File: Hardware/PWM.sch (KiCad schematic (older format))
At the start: 7 parts, among them P1 PWM, U1 NLAS4599

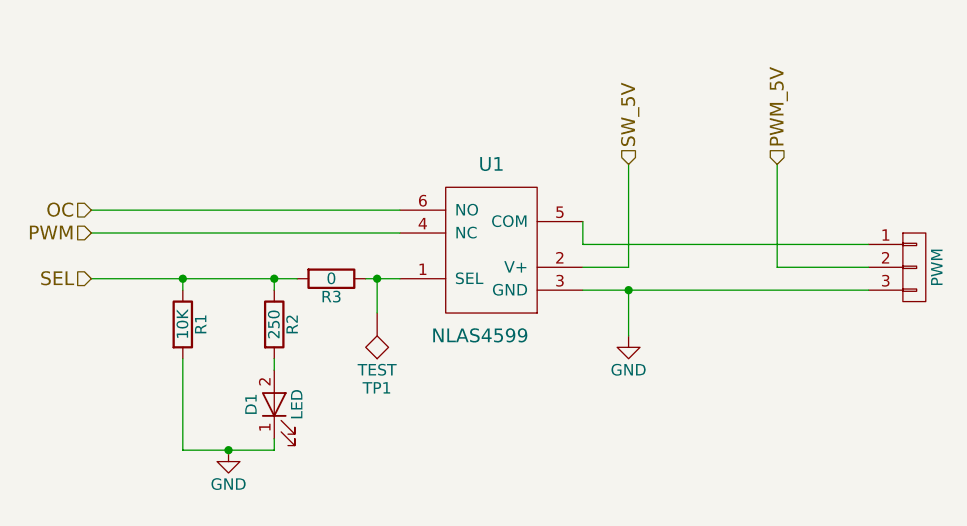
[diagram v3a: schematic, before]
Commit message: Added F0 chip
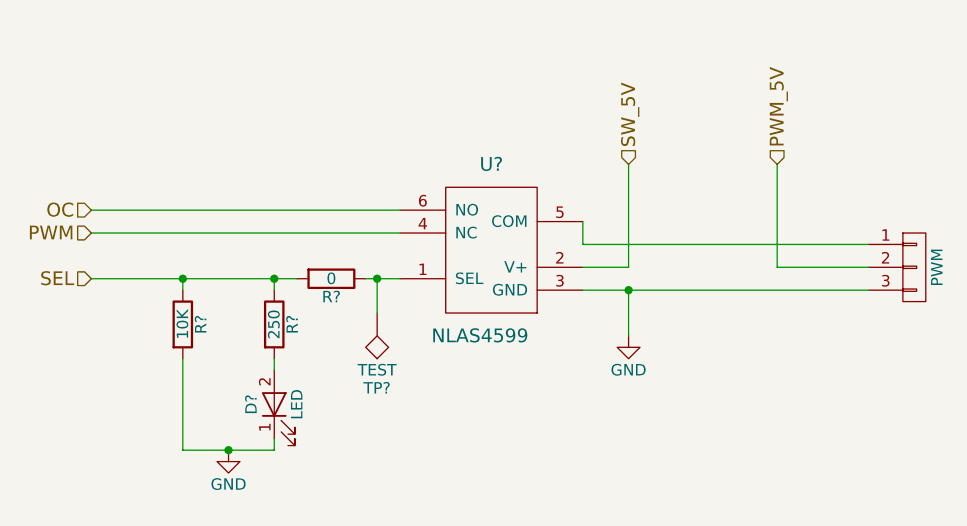
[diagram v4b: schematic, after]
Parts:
- renumbered D1 to D?, P1 to P?, R2 to R?, R34 to R?, R36 to R?, TP12 to TP?, U1 to U?
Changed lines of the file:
@@
 $Descr A4 11693 8268
 encoding utf-8
-Sheet 3 17
+Sheet 8 18
 Title "PWM Switching Circuit"
 Date "2017-05-13"
@@
 U 1 1 5917D576
 P 6350 2400
-AR Path="/5917CEAC/5917D576" Ref="P?"  Part="1"
-AR Path="/5917EAD8/5917D576" Ref="P?"  Part="1"
-AR Path="/5917F7DD/5917D576" Ref="P?"  Part="1"
-AR Path="/591836F4/5917D576" Ref="P?"  Part="1"
-AR Path="/5919E173/5917D576" Ref="P?"  Part="1"
-AR Path="/591E6415/591EA448/5917D576" Ref="P1"  Part="1"
-AR Path="/591E6415/591EA45A/5917D576" Ref="P2"  Part="1"
-AR Path="/591E6415/591EA50E/5917D576" Ref="P12"  Part="1"
-AR Path="/591E6415/591EA490/5917D576" Ref="P5"  Part="1"
-AR Path="/591E6415/591EA46C/5917D576" Ref="P3"  Part="1"
-AR Path="/591E6415/591EA47E/5917D576" Ref="P4"  Part="1"
-AR Path="/591E6415/591EA4A2/5917D576" Ref="P6"  Part="1"
-AR Path="/591E6415/591EA4B4/5917D576" Ref="P7"  Part="1"
-AR Path="/591E6415/591EA4C6/5917D576" Ref="P8"  Part="1"
-AR Path="/591E6415/591EA4D8/5917D576" Ref="P9"  Part="1"
-AR Path="/591E6415/591EA4EA/5917D576" Ref="P10"  Part="1"
-AR Path="/591E6415/591EA4FC/5917D576" Ref="P11"  Part="1"
-F 0 "P1" H 6350 2600 50  0001 C CNN
+F 0 "P?" H 6350 2600 50  0001 C CNN
 F 1 "PWM" V 6450 2400 50  0000 C CNN
 F 2 "" H 6350 2400 50  0000 C CNN
@@
 $EndComp
 $Comp
-L NLAS4599 U1
+L NLAS4599 U?
 U 1 1 5917D57C
 P 4500 2600
-AR Path="/5917CEAC/5917D57C" Ref="U1"  Part="1"
-AR Path="/5917EAD8/5917D57C" Ref="U1"  Part="1"
-AR Path="/5917F7DD/5917D57C" Ref="U1"  Part="1"
-AR Path="/591836F4/5917D57C" Ref="U1"  Part="1"
-AR Path="/5919E173/5917D57C" Ref="U1"  Part="1"
-AR Path="/591E6415/591EA448/5917D57C" Ref="U?"  Part="1"
-AR Path="/591E6415/591EA45A/5917D57C" Ref="U1"  Part="1"
-AR Path="/591E6415/591EA50E/5917D57C" Ref="U1"  Part="1"
-AR Path="/591E6415/591EA490/5917D57C" Ref="U1"  Part="1"
-AR Path="/591E6415/591EA46C/5917D57C" Ref="U1"  Part="1"
-AR Path="/591E6415/591EA47E/5917D57C" Ref="U1"  Part="1"
-AR Path="/591E6415/591EA4A2/5917D57C" Ref="U1"  Part="1"
-AR Path="/591E6415/591EA4B4/5917D57C" Ref="U1"  Part="1"
-AR Path="/591E6415/591EA4C6/5917D57C" Ref="U1"  Part="1"
-AR Path="/591E6415/591EA4D8/5917D57C" Ref="U1"  Part="1"
-AR Path="/591E6415/591EA4EA/5917D57C" Ref="U1"  Part="1"
-AR Path="/591E6415/591EA4FC/5917D57C" Ref="U1"  Part="1"
 F 0 "U?" H 4500 3250 60  0000 C CNN
 F 1 "NLAS4599" H 4550 2500 60  0000 C CNN
@@
 U 1 1 5917D836
 P 5100 2700
-AR Path="/5917CEAC/5917D836" Ref="#PWR?"  Part="1"
-AR Path="/5917EAD8/5917D836" Ref="#PWR?"  Part="1"
-AR Path="/5917F7DD/5917D836" Ref="#PWR?"  Part="1"
-AR Path="/591836F4/5917D836" Ref="#PWR?"  Part="1"
-AR Path="/5919E173/5917D836" Ref="#PWR?"  Part="1"
-AR Path="/591E6415/591EA448/5917D836" Ref="#PWR2"  Part="1"
-AR Path="/591E6415/591EA45A/5917D836" Ref="#PWR4"  Part="1"
-AR Path="/591E6415/591EA50E/5917D836" Ref="#PWR24"  Part="1"
-AR Path="/591E6415/591EA490/5917D836" Ref="#PWR10"  Part="1"
-AR Path="/591E6415/591EA46C/5917D836" Ref="#PWR6"  Part="1"
-AR Path="/591E6415/591EA47E/5917D836" Ref="#PWR8"  Part="1"
-AR Path="/591E6415/591EA4A2/5917D836" Ref="#PWR12"  Part="1"
-AR Path="/591E6415/591EA4B4/5917D836" Ref="#PWR14"  Part="1"
-AR Path="/591E6415/591EA4C6/5917D836" Ref="#PWR16"  Part="1"
-AR Path="/591E6415/591EA4D8/5917D836" Ref="#PWR18"  Part="1"
-AR Path="/591E6415/591EA4EA/5917D836" Ref="#PWR20"  Part="1"
-AR Path="/591E6415/591EA4FC/5917D836" Ref="#PWR22"  Part="1"
-F 0 "#PWR2" H 5100 2450 50  0001 C CNN
+F 0 "#PWR?" H 5100 2450 50  0001 C CNN
 F 1 "GND" H 5100 2550 50  0000 C CNN
 F 2 "" H 5100 2700 50  0000 C CNN
@@
 	4900 2300 6150 2300
 $Comp
-L LED D1
+L LED D?
 U 1 1 591EF19A
 P 3550 3000
-AR Path="/591E6415/591EA448/591EF19A" Ref="D1"  Part="1"
-AR Path="/591E6415/591EA50E/591EF19A" Ref="D12"  Part="1"
-AR Path="/591E6415/591EA490/591EF19A" Ref="D5"  Part="1"
-AR Path="/591E6415/591EA45A/591EF19A" Ref="D2"  Part="1"
-AR Path="/591E6415/591EA46C/591EF19A" Ref="D3"  Part="1"
-AR Path="/591E6415/591EA47E/591EF19A" Ref="D4"  Part="1"
-AR Path="/591E6415/591EA4A2/591EF19A" Ref="D6"  Part="1"
-AR Path="/591E6415/591EA4B4/591EF19A" Ref="D7"  Part="1"
-AR Path="/591E6415/591EA4C6/591EF19A" Ref="D8"  Part="1"
-AR Path="/591E6415/591EA4D8/591EF19A" Ref="D9"  Part="1"
-AR Path="/591E6415/591EA4EA/591EF19A" Ref="D10"  Part="1"
-AR Path="/591E6415/591EA4FC/591EF19A" Ref="D11"  Part="1"
-F 0 "D1" H 3550 3100 50  0000 C CNN
+F 0 "D?" H 3550 3100 50  0000 C CNN
 F 1 "LED" H 3550 2900 50  0000 C CNN
 F 2 "" H 3550 3000 50  0000 C CNN
@@
 $EndComp
 $Comp
-L R R2
+L R R?
 U 1 1 591EF2D3
 P 3550 2650
-AR Path="/591E6415/591EA448/591EF2D3" Ref="R2"  Part="1"
-AR Path="/591E6415/591EA50E/591EF2D3" Ref="R35"  Part="1"
-AR Path="/591E6415/591EA490/591EF2D3" Ref="R14"  Part="1"
-AR Path="/591E6415/591EA45A/591EF2D3" Ref="R5"  Part="1"
-AR Path="/591E6415/591EA46C/591EF2D3" Ref="R8"  Part="1"
-AR Path="/591E6415/591EA47E/591EF2D3" Ref="R11"  Part="1"
-AR Path="/591E6415/591EA4A2/591EF2D3" Ref="R17"  Part="1"
-AR Path="/591E6415/591EA4B4/591EF2D3" Ref="R20"  Part="1"
-AR Path="/591E6415/591EA4C6/591EF2D3" Ref="R23"  Part="1"
-AR Path="/591E6415/591EA4D8/591EF2D3" Ref="R26"  Part="1"
-AR Path="/591E6415/591EA4EA/591EF2D3" Ref="R29"  Part="1"
-AR Path="/591E6415/591EA4FC/591EF2D3" Ref="R32"  Part="1"
-F 0 "R2" V 3630 2650 50  0000 C CNN
+F 0 "R?" V 3630 2650 50  0000 C CNN
 F 1 "250" V 3550 2650 50  0000 C CNN
 F 2 "" V 3480 2650 50  0000 C CNN
@@
 Connection ~ 3550 2450
 $Comp
-L GND #PWR1
+L GND #PWR?
 U 1 1 591EF3D9
 P 3350 3200
-AR Path="/591E6415/591EA448/591EF3D9" Ref="#PWR1"  Part="1"
-AR Path="/591E6415/591EA50E/591EF3D9" Ref="#PWR23"  Part="1"
-AR Path="/591E6415/591EA490/591EF3D9" Ref="#PWR9"  Part="1"
-AR Path="/591E6415/591EA45A/591EF3D9" Ref="#PWR3"  Part="1"
-AR Path="/591E6415/591EA46C/591EF3D9" Ref="#PWR5"  Part="1"
-AR Path="/591E6415/591EA47E/591EF3D9" Ref="#PWR7"  Part="1"
-AR Path="/591E6415/591EA4A2/591EF3D9" Ref="#PWR11"  Part="1"
-AR Path="/591E6415/591EA4B4/591EF3D9" Ref="#PWR13"  Part="1"
-AR Path="/591E6415/591EA4C6/591EF3D9" Ref="#PWR15"  Part="1"
-AR Path="/591E6415/591EA4D8/591EF3D9" Ref="#PWR17"  Part="1"
-AR Path="/591E6415/591EA4EA/591EF3D9" Ref="#PWR19"  Part="1"
-AR Path="/591E6415/591EA4FC/591EF3D9" Ref="#PWR21"  Part="1"
-F 0 "#PWR1" H 3350 2950 50  0001 C CNN
+F 0 "#PWR?" H 3350 2950 50  0001 C CNN
 F 1 "GND" H 3350 3050 50  0000 C CNN
 F 2 "" H 3350 3200 50  0000 C CNN
@@
 	3550 3200 3550 3150
 $Comp
-L R R34
+L R R?
 U 1 1 591F0A89
 P 3150 2650
-AR Path="/591E6415/591EA50E/591F0A89" Ref="R34"  Part="1"
-AR Path="/591E6415/591EA448/591F0A89" Ref="R1"  Part="1"
-AR Path="/591E6415/591EA45A/591F0A89" Ref="R4"  Part="1"
-AR Path="/591E6415/591EA46C/591F0A89" Ref="R7"  Part="1"
-AR Path="/591E6415/591EA47E/591F0A89" Ref="R10"  Part="1"
-AR Path="/591E6415/591EA490/591F0A89" Ref="R13"  Part="1"
-AR Path="/591E6415/591EA4A2/591F0A89" Ref="R16"  Part="1"
-AR Path="/591E6415/591EA4B4/591F0A89" Ref="R19"  Part="1"
-AR Path="/591E6415/591EA4C6/591F0A89" Ref="R22"  Part="1"
-AR Path="/591E6415/591EA4D8/591F0A89" Ref="R25"  Part="1"
-AR Path="/591E6415/591EA4EA/591F0A89" Ref="R28"  Part="1"
-AR Path="/591E6415/591EA4FC/591F0A89" Ref="R31"  Part="1"
-F 0 "R1" V 3230 2650 50  0000 C CNN
+F 0 "R?" V 3230 2650 50  0000 C CNN
 F 1 "10K" V 3150 2650 50  0000 C CNN
 F 2 "" V 3080 2650 50  0000 C CNN
@@
 Connection ~ 3150 2450
 $Comp
-L R R36
+L R R?
 U 1 1 591F0BAE
 P 3800 2450
-AR Path="/591E6415/591EA50E/591F0BAE" Ref="R36"  Part="1"
-AR Path="/591E6415/591EA448/591F0BAE" Ref="R3"  Part="1"
-AR Path="/591E6415/591EA45A/591F0BAE" Ref="R6"  Part="1"
-AR Path="/591E6415/591EA46C/591F0BAE" Ref="R9"  Part="1"
-AR Path="/591E6415/591EA47E/591F0BAE" Ref="R12"  Part="1"
-AR Path="/591E6415/591EA490/591F0BAE" Ref="R15"  Part="1"
-AR Path="/591E6415/591EA4A2/591F0BAE" Ref="R18"  Part="1"
-AR Path="/591E6415/591EA4B4/591F0BAE" Ref="R21"  Part="1"
-AR Path="/591E6415/591EA4C6/591F0BAE" Ref="R24"  Part="1"
-AR Path="/591E6415/591EA4D8/591F0BAE" Ref="R27"  Part="1"
-AR Path="/591E6415/591EA4EA/591F0BAE" Ref="R30"  Part="1"
-AR Path="/591E6415/591EA4FC/591F0BAE" Ref="R33"  Part="1"
-F 0 "R3" V 3880 2450 50  0000 C CNN
+F 0 "R?" V 3880 2450 50  0000 C CNN
 F 1 "0" V 3800 2450 50  0000 C CNN
 F 2 "" V 3730 2450 50  0000 C CNN
@@
 Connection ~ 4000 2450
 $Comp
-L TEST TP12
+L TEST TP?
 U 1 1 591F0CEF
 P 4000 2600
-AR Path="/591E6415/591EA50E/591F0CEF" Ref="TP12"  Part="1"
-AR Path="/591E6415/591EA448/591F0CEF" Ref="TP1"  Part="1"
-AR Path="/591E6415/591EA45A/591F0CEF" Ref="TP2"  Part="1"
-AR Path="/591E6415/591EA46C/591F0CEF" Ref="TP3"  Part="1"
-AR Path="/591E6415/591EA47E/591F0CEF" Ref="TP4"  Part="1"
-AR Path="/591E6415/591EA490/591F0CEF" Ref="TP5"  Part="1"
-AR Path="/591E6415/591EA4A2/591F0CEF" Ref="TP6"  Part="1"
-AR Path="/591E6415/591EA4B4/591F0CEF" Ref="TP7"  Part="1"
-AR Path="/591E6415/591EA4C6/591F0CEF" Ref="TP8"  Part="1"
-AR Path="/591E6415/591EA4D8/591F0CEF" Ref="TP9"  Part="1"
-AR Path="/591E6415/591EA4EA/591F0CEF" Ref="TP10"  Part="1"
-AR Path="/591E6415/591EA4FC/591F0CEF" Ref="TP11"  Part="1"
-F 0 "TP1" H 4000 2900 50  0000 C BNN
+F 0 "TP?" H 4000 2900 50  0000 C BNN
 F 1 "TEST" H 4000 2850 50  0000 C CNN
 F 2 "" H 4000 2600 50  0000 C CNN

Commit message: Added F7 Circuitry
Added way too much for 1 commit.
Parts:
- gave numbers to parts that had none: 7
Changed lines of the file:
@@
 LIBS:contrib
 LIBS:valves
+LIBS:ZeroPilot-cache
 EELAYER 25 0
 EELAYER END
 $Descr A4 11693 8268
 encoding utf-8
-Sheet 8 18
+Sheet 6 17
 Title "PWM Switching Circuit"
 Date "2017-05-13"
@@
 $EndDescr
 $Comp
-L CONN_01X03 P?
+L CONN_01X03 P1
 U 1 1 5917D576
 P 6350 2400
-F 0 "P?" H 6350 2600 50  0001 C CNN
+AR Path="/591E6415/591EA448/5917D576" Ref="P1"  Part="1"
+AR Path="/591E6415/591EA45A/5917D576" Ref="P2"  Part="1"
+AR Path="/591E6415/591EA46C/5917D576" Ref="P3"  Part="1"
+AR Path="/591E6415/591EA47E/5917D576" Ref="P4"  Part="1"
+AR Path="/591E6415/591EA490/5917D576" Ref="P5"  Part="1"
+AR Path="/591E6415/591EA4A2/5917D576" Ref="P6"  Part="1"
+AR Path="/591E6415/591EA4B4/5917D576" Ref="P7"  Part="1"
+AR Path="/591E6415/591EA4C6/5917D576" Ref="P8"  Part="1"
+AR Path="/591E6415/591EA4D8/5917D576" Ref="P9"  Part="1"
+AR Path="/591E6415/591EA4EA/5917D576" Ref="P10"  Part="1"
+AR Path="/591E6415/591EA4FC/5917D576" Ref="P11"  Part="1"
+AR Path="/591E6415/591EA50E/5917D576" Ref="P12"  Part="1"
+F 0 "P4" H 6350 2600 50  0001 C CNN
 F 1 "PWM" V 6450 2400 50  0000 C CNN
 F 2 "" H 6350 2400 50  0000 C CNN
@@
 $EndComp
 $Comp
-L NLAS4599 U?
+L NLAS4599 U1
 U 1 1 5917D57C
 P 4500 2600
-F 0 "U?" H 4500 3250 60  0000 C CNN
+AR Path="/591E6415/591EA448/5917D57C" Ref="U1"  Part="1"
+AR Path="/591E6415/591EA45A/5917D57C" Ref="U2"  Part="1"
+AR Path="/591E6415/591EA46C/5917D57C" Ref="U3"  Part="1"
+AR Path="/591E6415/591EA47E/5917D57C" Ref="U4"  Part="1"
+AR Path="/591E6415/591EA490/5917D57C" Ref="U5"  Part="1"
+AR Path="/591E6415/591EA4A2/5917D57C" Ref="U6"  Part="1"
+AR Path="/591E6415/591EA4B4/5917D57C" Ref="U7"  Part="1"
+AR Path="/591E6415/591EA4C6/5917D57C" Ref="U8"  Part="1"
+AR Path="/591E6415/591EA4D8/5917D57C" Ref="U9"  Part="1"
+AR Path="/591E6415/591EA4EA/5917D57C" Ref="U10"  Part="1"
+AR Path="/591E6415/591EA4FC/5917D57C" Ref="U11"  Part="1"
+AR Path="/591E6415/591EA50E/5917D57C" Ref="U12"  Part="1"
+F 0 "U4" H 4500 3250 60  0000 C CNN
 F 1 "NLAS4599" H 4550 2500 60  0000 C CNN
 F 2 "" H 4300 2350 60  0001 C CNN
@@
 	4900 2500 6150 2500
 $Comp
-L GND #PWR?
+L GND #PWR01
 U 1 1 5917D836
 P 5100 2700
-F 0 "#PWR?" H 5100 2450 50  0001 C CNN
+AR Path="/591E6415/591EA448/5917D836" Ref="#PWR01"  Part="1"
+AR Path="/591E6415/591EA45A/5917D836" Ref="#PWR03"  Part="1"
+AR Path="/591E6415/591EA46C/5917D836" Ref="#PWR05"  Part="1"
+AR Path="/591E6415/591EA47E/5917D836" Ref="#PWR07"  Part="1"
+AR Path="/591E6415/591EA490/5917D836" Ref="#PWR09"  Part="1"
+AR Path="/591E6415/591EA4A2/5917D836" Ref="#PWR011"  Part="1"
+AR Path="/591E6415/591EA4B4/5917D836" Ref="#PWR013"  Part="1"
+AR Path="/591E6415/591EA4C6/5917D836" Ref="#PWR015"  Part="1"
+AR Path="/591E6415/591EA4D8/5917D836" Ref="#PWR017"  Part="1"
+AR Path="/591E6415/591EA4EA/5917D836" Ref="#PWR019"  Part="1"
+AR Path="/591E6415/591EA4FC/5917D836" Ref="#PWR021"  Part="1"
+AR Path="/591E6415/591EA50E/5917D836" Ref="#PWR023"  Part="1"
+F 0 "#PWR07" H 5100 2450 50  0001 C CNN
 F 1 "GND" H 5100 2550 50  0000 C CNN
 F 2 "" H 5100 2700 50  0000 C CNN
@@
 	5750 2400 5750 1950
 Connection ~ 5100 2500
-Wire Wire Line
-	4900 2400 5100 2400
 Wire Wire Line
 	5100 2700 5100 2500
@@
 	4900 2300 6150 2300
 $Comp
-L LED D?
+L LED D1
 U 1 1 591EF19A
 P 3550 3000
-F 0 "D?" H 3550 3100 50  0000 C CNN
+AR Path="/591E6415/591EA448/591EF19A" Ref="D1"  Part="1"
+AR Path="/591E6415/591EA45A/591EF19A" Ref="D2"  Part="1"
+AR Path="/591E6415/591EA46C/591EF19A" Ref="D3"  Part="1"
+AR Path="/591E6415/591EA47E/591EF19A" Ref="D4"  Part="1"
+AR Path="/591E6415/591EA490/591EF19A" Ref="D5"  Part="1"
+AR Path="/591E6415/591EA4A2/591EF19A" Ref="D6"  Part="1"
+AR Path="/591E6415/591EA4B4/591EF19A" Ref="D7"  Part="1"
+AR Path="/591E6415/591EA4C6/591EF19A" Ref="D8"  Part="1"
+AR Path="/591E6415/591EA4D8/591EF19A" Ref="D9"  Part="1"
+AR Path="/591E6415/591EA4EA/591EF19A" Ref="D10"  Part="1"
+AR Path="/591E6415/591EA4FC/591EF19A" Ref="D11"  Part="1"
+AR Path="/591E6415/591EA50E/591EF19A" Ref="D12"  Part="1"
+F 0 "D4" H 3550 3100 50  0000 C CNN
 F 1 "LED" H 3550 2900 50  0000 C CNN
 F 2 "" H 3550 3000 50  0000 C CNN
@@
 $EndComp
 $Comp
-L R R?
+L R R2
 U 1 1 591EF2D3
 P 3550 2650
-F 0 "R?" V 3630 2650 50  0000 C CNN
+AR Path="/591E6415/591EA448/591EF2D3" Ref="R2"  Part="1"
+AR Path="/591E6415/591EA45A/591EF2D3" Ref="R5"  Part="1"
+AR Path="/591E6415/591EA46C/591EF2D3" Ref="R8"  Part="1"
+AR Path="/591E6415/591EA47E/591EF2D3" Ref="R11"  Part="1"
+AR Path="/591E6415/591EA490/591EF2D3" Ref="R14"  Part="1"
+AR Path="/591E6415/591EA4A2/591EF2D3" Ref="R17"  Part="1"
+AR Path="/591E6415/591EA4B4/591EF2D3" Ref="R20"  Part="1"
+AR Path="/591E6415/591EA4C6/591EF2D3" Ref="R23"  Part="1"
+AR Path="/591E6415/591EA4D8/591EF2D3" Ref="R26"  Part="1"
+AR Path="/591E6415/591EA4EA/591EF2D3" Ref="R29"  Part="1"
+AR Path="/591E6415/591EA4FC/591EF2D3" Ref="R32"  Part="1"
+AR Path="/591E6415/591EA50E/591EF2D3" Ref="R35"  Part="1"
+F 0 "R11" V 3630 2650 50  0000 C CNN
 F 1 "250" V 3550 2650 50  0000 C CNN
 F 2 "" V 3480 2650 50  0000 C CNN
@@
 Connection ~ 3550 2450
 $Comp
-L GND #PWR?
+L GND #PWR02
 U 1 1 591EF3D9
-P 3350 3200
-F 0 "#PWR?" H 3350 2950 50  0001 C CNN
-F 1 "GND" H 3350 3050 50  0000 C CNN
-F 2 "" H 3350 3200 50  0000 C CNN
-F 3 "" H 3350 3200 50  0000 C CNN
-	1    3350 3200
+P 3350 3250
+AR Path="/591E6415/591EA448/591EF3D9" Ref="#PWR02"  Part="1"
+AR Path="/591E6415/591EA45A/591EF3D9" Ref="#PWR04"  Part="1"
+AR Path="/591E6415/591EA46C/591EF3D9" Ref="#PWR06"  Part="1"
+AR Path="/591E6415/591EA47E/591EF3D9" Ref="#PWR08"  Part="1"
+AR Path="/591E6415/591EA490/591EF3D9" Ref="#PWR010"  Part="1"
+AR Path="/591E6415/591EA4A2/591EF3D9" Ref="#PWR012"  Part="1"
+AR Path="/591E6415/591EA4B4/591EF3D9" Ref="#PWR014"  Part="1"
+AR Path="/591E6415/591EA4C6/591EF3D9" Ref="#PWR016"  Part="1"
+AR Path="/591E6415/591EA4D8/591EF3D9" Ref="#PWR018"  Part="1"
+AR Path="/591E6415/591EA4EA/591EF3D9" Ref="#PWR020"  Part="1"
+AR Path="/591E6415/591EA4FC/591EF3D9" Ref="#PWR022"  Part="1"
+AR Path="/591E6415/591EA50E/591EF3D9" Ref="#PWR024"  Part="1"
+F 0 "#PWR08" H 3350 3000 50  0001 C CNN
+F 1 "GND" H 3350 3100 50  0000 C CNN
+F 2 "" H 3350 3250 50  0000 C CNN
+F 3 "" H 3350 3250 50  0000 C CNN
+	1    3350 3250
 	1    0    0    -1
 $EndComp
@@
 	3550 3200 3550 3150
 $Comp
-L R R?
+L R R1
 U 1 1 591F0A89
 P 3150 2650
-F 0 "R?" V 3230 2650 50  0000 C CNN
+AR Path="/591E6415/591EA448/591F0A89" Ref="R1"  Part="1"
+AR Path="/591E6415/591EA45A/591F0A89" Ref="R4"  Part="1"
+AR Path="/591E6415/591EA46C/591F0A89" Ref="R7"  Part="1"
+AR Path="/591E6415/591EA47E/591F0A89" Ref="R10"  Part="1"
+AR Path="/591E6415/591EA490/591F0A89" Ref="R13"  Part="1"
+AR Path="/591E6415/591EA4A2/591F0A89" Ref="R16"  Part="1"
+AR Path="/591E6415/591EA4B4/591F0A89" Ref="R19"  Part="1"
+AR Path="/591E6415/591EA4C6/591F0A89" Ref="R22"  Part="1"
+AR Path="/591E6415/591EA4D8/591F0A89" Ref="R25"  Part="1"
+AR Path="/591E6415/591EA4EA/591F0A89" Ref="R28"  Part="1"
+AR Path="/591E6415/591EA4FC/591F0A89" Ref="R31"  Part="1"
+AR Path="/591E6415/591EA50E/591F0A89" Ref="R34"  Part="1"
+F 0 "R10" V 3230 2650 50  0000 C CNN
 F 1 "10K" V 3150 2650 50  0000 C CNN
 F 2 "" V 3080 2650 50  0000 C CNN
@@
 Wire Wire Line
 	3150 2800 3150 3200
-Connection ~ 3350 3200
 Wire Wire Line
 	3150 2500 3150 2450
 Connection ~ 3150 2450
 $Comp
-L R R?
+L R R3
 U 1 1 591F0BAE
 P 3800 2450
-F 0 "R?" V 3880 2450 50  0000 C CNN
+AR Path="/591E6415/591EA448/591F0BAE" Ref="R3"  Part="1"
+AR Path="/591E6415/591EA45A/591F0BAE" Ref="R6"  Part="1"
+AR Path="/591E6415/591EA46C/591F0BAE" Ref="R9"  Part="1"
+AR Path="/591E6415/591EA47E/591F0BAE" Ref="R12"  Part="1"
+AR Path="/591E6415/591EA490/591F0BAE" Ref="R15"  Part="1"
+AR Path="/591E6415/591EA4A2/591F0BAE" Ref="R18"  Part="1"
+AR Path="/591E6415/591EA4B4/591F0BAE" Ref="R21"  Part="1"
+AR Path="/591E6415/591EA4C6/591F0BAE" Ref="R24"  Part="1"
+AR Path="/591E6415/591EA4D8/591F0BAE" Ref="R27"  Part="1"
+AR Path="/591E6415/591EA4EA/591F0BAE" Ref="R30"  Part="1"
+AR Path="/591E6415/591EA4FC/591F0BAE" Ref="R33"  Part="1"
+AR Path="/591E6415/591EA50E/591F0BAE" Ref="R36"  Part="1"
+F 0 "R12" V 3880 2450 50  0000 C CNN
 F 1 "0" V 3800 2450 50  0000 C CNN
 F 2 "" V 3730 2450 50  0000 C CNN
@@
 Connection ~ 4000 2450
 $Comp
-L TEST TP?
+L TEST TP1
 U 1 1 591F0CEF
 P 4000 2600
-F 0 "TP?" H 4000 2900 50  0000 C BNN
+AR Path="/591E6415/591EA448/591F0CEF" Ref="TP1"  Part="1"
+AR Path="/591E6415/591EA45A/591F0CEF" Ref="TP2"  Part="1"
+AR Path="/591E6415/591EA46C/591F0CEF" Ref="TP3"  Part="1"
+AR Path="/591E6415/591EA47E/591F0CEF" Ref="TP4"  Part="1"
+AR Path="/591E6415/591EA490/591F0CEF" Ref="TP5"  Part="1"
+AR Path="/591E6415/591EA4A2/591F0CEF" Ref="TP6"  Part="1"
+AR Path="/591E6415/591EA4B4/591F0CEF" Ref="TP7"  Part="1"
+AR Path="/591E6415/591EA4C6/591F0CEF" Ref="TP8"  Part="1"
+AR Path="/591E6415/591EA4D8/591F0CEF" Ref="TP9"  Part="1"
+AR Path="/591E6415/591EA4EA/591F0CEF" Ref="TP10"  Part="1"
+AR Path="/591E6415/591EA4FC/591F0CEF" Ref="TP11"  Part="1"
+AR Path="/591E6415/591EA50E/591F0CEF" Ref="TP12"  Part="1"
+F 0 "TP4" H 4000 2900 50  0000 C BNN
 F 1 "TEST" H 4000 2850 50  0000 C CNN
 F 2 "" H 4000 2600 50  0000 C CNN
@@
 Wire Wire Line
 	5100 2400 5100 1950
+Wire Wire Line
+	3350 3200 3350 3250
+Connection ~ 3350 3200
+Wire Wire Line
+	5100 2400 4900 2400
 $EndSCHEMATC
